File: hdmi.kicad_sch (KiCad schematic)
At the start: 11 parts, among them J2101 FPC0.5-SMT-20P, U2101 RCLAMP0524P, U2102 RCLAMP0524P, U2103 RCLAMP0524P, U3102 AP22653W6-7

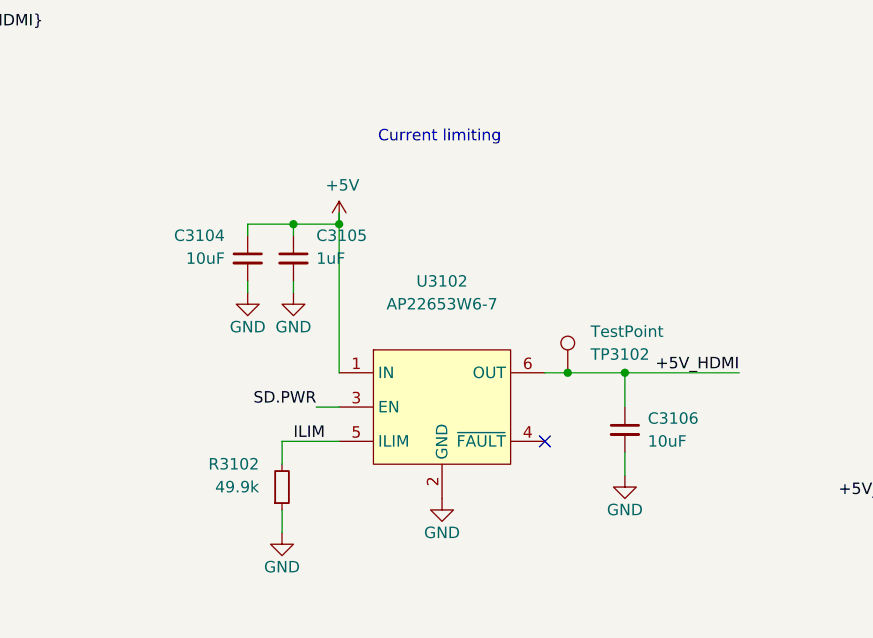
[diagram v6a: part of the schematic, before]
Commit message: Finish transitioning to RP2040
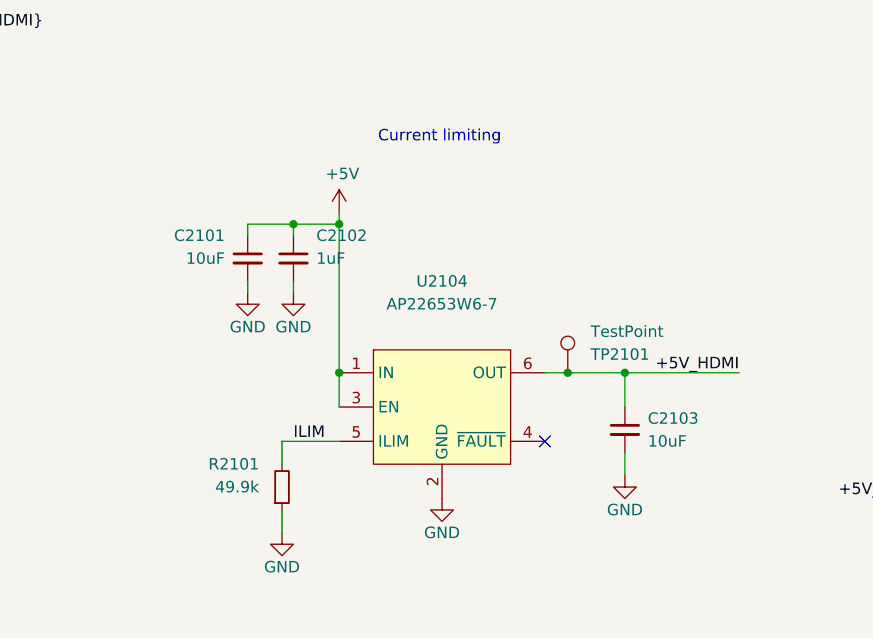
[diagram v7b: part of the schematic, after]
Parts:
- renumbered C3104 to C2101, C3105 to C2102, C3106 to C2103, R3102 to R2101, TP3102 to TP2101, U3102 to U2104
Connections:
- net SD.PWR is gone; now on net +5V: U2104.3 (EN)
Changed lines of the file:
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@@
 	)
 	(junction
+		(at 148.59 99.06)
+		(diameter 0)
+		(color 0 0 0 0)
+	)
+	(junction
 		(at 180.34 99.06)
 		(diameter 0.9144)
@@
 	(wire
 		(pts
-			(xy 146.05 102.87) (xy 148.59 102.87)
-		)
-		(stroke
-			(width 0)
-			(type default)
-		)
-	)
-	(wire
-		(pts
 			(xy 242.57 73.66) (xy 242.57 81.28)
 		)
@@
 	(wire
 		(pts
+			(xy 148.59 99.06) (xy 148.59 102.87)
+		)
+		(stroke
+			(width 0)
+			(type default)
+		)
+	)
+	(wire
+		(pts
 			(xy 213.36 113.03) (xy 217.17 113.03)
 		)
@@
 		)
 	)
-	(label "SD.PWR"
-		(at 146.05 102.87 180)
-		(effects
-			(font
-				(size 1.27 1.27)
-			)
-			(justify right bottom)
-		)
-	)
 	(label "HDMI.D0-"
 		(at 97.79 107.95 180)
@@
 		(dnp no)
 		(fields_autoplaced yes)
-		(property "Reference" "R3102"
+		(property "Reference" "R2101"
 			(at 139.7 109.2199 0)
 			(effects
@@
 			(project "HALPI2"
 				(path "/abc482bd-3f17-4d35-80db-1da3dcdb5c27/851e7ce4-d5b0-47f7-ace9-4a347f172348/49314faa-db35-4ef5-b0c8-5c327f44891d"
-					(reference "R3103")
+					(reference "R2201")
 					(unit 1)
 				)
 				(path "/abc482bd-3f17-4d35-80db-1da3dcdb5c27/851e7ce4-d5b0-47f7-ace9-4a347f172348/890900ed-b859-477a-afc8-e6aecd491b67"
-					(reference "R3102")
+					(reference "R2101")
 					(unit 1)
 				)
@@
 		(on_board yes)
 		(dnp no)
-		(property "Reference" "#PWR03110"
+		(property "Reference" "#PWR02105"
 			(at 142.24 123.19 0)
 			(effects
@@
 			(project "HALPI2"
 				(path "/abc482bd-3f17-4d35-80db-1da3dcdb5c27/851e7ce4-d5b0-47f7-ace9-4a347f172348/49314faa-db35-4ef5-b0c8-5c327f44891d"
-					(reference "#PWR03116")
+					(reference "#PWR02205")
 					(unit 1)
 				)
 				(path "/abc482bd-3f17-4d35-80db-1da3dcdb5c27/851e7ce4-d5b0-47f7-ace9-4a347f172348/890900ed-b859-477a-afc8-e6aecd491b67"
-					(reference "#PWR03110")
+					(reference "#PWR02105")
 					(unit 1)
 				)
@@
 		(on_board yes)
 		(dnp no)
-		(property "Reference" "#PWR02107"
+		(property "Reference" "#PWR02112"
 			(at 256.54 69.85 0)
 			(effects
@@
 			(project "HALPI2"
 				(path "/abc482bd-3f17-4d35-80db-1da3dcdb5c27/851e7ce4-d5b0-47f7-ace9-4a347f172348/49314faa-db35-4ef5-b0c8-5c327f44891d"
-					(reference "#PWR02207")
+					(reference "#PWR02212")
 					(unit 1)
 				)
 				(path "/abc482bd-3f17-4d35-80db-1da3dcdb5c27/851e7ce4-d5b0-47f7-ace9-4a347f172348/890900ed-b859-477a-afc8-e6aecd491b67"
-					(reference "#PWR02107")
+					(reference "#PWR02112")
 					(unit 1)
 				)
@@
 		(on_board yes)
 		(dnp no)
-		(property "Reference" "#PWR02106"
+		(property "Reference" "#PWR02111"
 			(at 242.57 133.35 0)
 			(effects
@@
 			(project "HALPI2"
 				(path "/abc482bd-3f17-4d35-80db-1da3dcdb5c27/851e7ce4-d5b0-47f7-ace9-4a347f172348/49314faa-db35-4ef5-b0c8-5c327f44891d"
-					(reference "#PWR02206")
+					(reference "#PWR02211")
 					(unit 1)
 				)
 				(path "/abc482bd-3f17-4d35-80db-1da3dcdb5c27/851e7ce4-d5b0-47f7-ace9-4a347f172348/890900ed-b859-477a-afc8-e6aecd491b67"
-					(reference "#PWR02106")
+					(reference "#PWR02111")
 					(unit 1)
 				)
@@
 		(dnp no)
 		(fields_autoplaced yes)
-		(property "Reference" "U3102"
+		(property "Reference" "U2104"
 			(at 160.02 88.9 0)
 			(effects
@@
 			(project "HALPI2"
 				(path "/abc482bd-3f17-4d35-80db-1da3dcdb5c27/851e7ce4-d5b0-47f7-ace9-4a347f172348/49314faa-db35-4ef5-b0c8-5c327f44891d"
-					(reference "U3103")
+					(reference "U2204")
 					(unit 1)
 				)
 				(path "/abc482bd-3f17-4d35-80db-1da3dcdb5c27/851e7ce4-d5b0-47f7-ace9-4a347f172348/890900ed-b859-477a-afc8-e6aecd491b67"
-					(reference "U3102")
+					(reference "U2104")
 					(unit 1)
 				)
@@
 		(on_board yes)
 		(dnp no)
-		(property "Reference" "TP3102"
+		(property "Reference" "TP2101"
 			(at 176.53 97.0281 0)
 			(effects
@@
 			(project "HALPI2"
 				(path "/abc482bd-3f17-4d35-80db-1da3dcdb5c27/851e7ce4-d5b0-47f7-ace9-4a347f172348/49314faa-db35-4ef5-b0c8-5c327f44891d"
-					(reference "TP3103")
+					(reference "TP2201")
 					(unit 1)
 				)
 				(path "/abc482bd-3f17-4d35-80db-1da3dcdb5c27/851e7ce4-d5b0-47f7-ace9-4a347f172348/890900ed-b859-477a-afc8-e6aecd491b67"
-					(reference "TP3102")
+					(reference "TP2101")
 					(unit 1)
 				)
@@
 		(on_board yes)
 		(dnp no)
-		(property "Reference" "C3106"
+		(property "Reference" "C2103"
 			(at 182.88 104.14 0)
 			(effects
@@
 			(project "HALPI2"
 				(path "/abc482bd-3f17-4d35-80db-1da3dcdb5c27/851e7ce4-d5b0-47f7-ace9-4a347f172348/49314faa-db35-4ef5-b0c8-5c327f44891d"
-					(reference "C3109")
+					(reference "C2203")
 					(unit 1)
 				)
 				(path "/abc482bd-3f17-4d35-80db-1da3dcdb5c27/851e7ce4-d5b0-47f7-ace9-4a347f172348/890900ed-b859-477a-afc8-e6aecd491b67"
-					(reference "C3106")
+					(reference "C2103")
 					(unit 1)
 				)
@@
 		(on_board yes)
 		(dnp no)
-		(property "Reference" "#PWR02105"
+		(property "Reference" "#PWR02110"
 			(at 217.17 133.35 0)
 			(effects
@@
 			(project "HALPI2"
 				(path "/abc482bd-3f17-4d35-80db-1da3dcdb5c27/851e7ce4-d5b0-47f7-ace9-4a347f172348/49314faa-db35-4ef5-b0c8-5c327f44891d"
-					(reference "#PWR02205")
+					(reference "#PWR02210")
 					(unit 1)
 				)
 				(path "/abc482bd-3f17-4d35-80db-1da3dcdb5c27/851e7ce4-d5b0-47f7-ace9-4a347f172348/890900ed-b859-477a-afc8-e6aecd491b67"
-					(reference "#PWR02105")
+					(reference "#PWR02110")
 					(unit 1)
 				)
@@
 		(dnp no)
 		(fields_autoplaced yes)
-		(property "Reference" "C3105"
+		(property "Reference" "C2102"
 			(at 146.05 83.8262 0)
 			(effects
@@
 			(project "HALPI2"
 				(path "/abc482bd-3f17-4d35-80db-1da3dcdb5c27/851e7ce4-d5b0-47f7-ace9-4a347f172348/49314faa-db35-4ef5-b0c8-5c327f44891d"
-					(reference "C3108")
+					(reference "C2202")
 					(unit 1)
 				)
 				(path "/abc482bd-3f17-4d35-80db-1da3dcdb5c27/851e7ce4-d5b0-47f7-ace9-4a347f172348/890900ed-b859-477a-afc8-e6aecd491b67"
-					(reference "C3105")
+					(reference "C2102")
 					(unit 1)
 				)
@@
 		(on_board yes)
 		(dnp no)
-		(property "Reference" "#PWR03114"
+		(property "Reference" "#PWR02109"
 			(at 180.34 116.84 0)
 			(effects
@@
 			(project "HALPI2"
 				(path "/abc482bd-3f17-4d35-80db-1da3dcdb5c27/851e7ce4-d5b0-47f7-ace9-4a347f172348/49314faa-db35-4ef5-b0c8-5c327f44891d"
-					(reference "#PWR03120")
+					(reference "#PWR02209")
 					(unit 1)
 				)
 				(path "/abc482bd-3f17-4d35-80db-1da3dcdb5c27/851e7ce4-d5b0-47f7-ace9-4a347f172348/890900ed-b859-477a-afc8-e6aecd491b67"
-					(reference "#PWR03114")
+					(reference "#PWR02109")
 					(unit 1)
 				)
@@
 		(on_board yes)
 		(dnp no)
-		(property "Reference" "#PWR03113"
+		(property "Reference" "#PWR02108"
 			(at 160.02 119.38 0)
 			(effects
@@
 			(project "HALPI2"
 				(path "/abc482bd-3f17-4d35-80db-1da3dcdb5c27/851e7ce4-d5b0-47f7-ace9-4a347f172348/49314faa-db35-4ef5-b0c8-5c327f44891d"
-					(reference "#PWR03119")
+					(reference "#PWR02208")
 					(unit 1)
 				)
 				(path "/abc482bd-3f17-4d35-80db-1da3dcdb5c27/851e7ce4-d5b0-47f7-ace9-4a347f172348/890900ed-b859-477a-afc8-e6aecd491b67"
-					(reference "#PWR03113")
+					(reference "#PWR02108")
 					(unit 1)
 				)
@@
 		(on_board yes)
 		(dnp no)
-		(property "Reference" "C3104"
+		(property "Reference" "C2101"
 			(at 135.89 83.8262 0)
 			(effects
@@
 			(project "HALPI2"
 				(path "/abc482bd-3f17-4d35-80db-1da3dcdb5c27/851e7ce4-d5b0-47f7-ace9-4a347f172348/49314faa-db35-4ef5-b0c8-5c327f44891d"
-					(reference "C3107")
+					(reference "C2201")
 					(unit 1)
 				)
 				(path "/abc482bd-3f17-4d35-80db-1da3dcdb5c27/851e7ce4-d5b0-47f7-ace9-4a347f172348/890900ed-b859-477a-afc8-e6aecd491b67"
-					(reference "C3104")
+					(reference "C2101")
 					(unit 1)
 				)
@@
 	(symbol
 		(lib_id "power:+5V")
-		(at 148.59 82.55 0)
+		(at 148.59 81.28 0)
 		(unit 1)
 		(exclude_from_sim no)
@@
 		(on_board yes)
 		(dnp no)
-		(property "Reference" "#PWR02108"
-			(at 148.59 86.36 0)
+		(property "Reference" "#PWR02107"
+			(at 148.59 85.09 0)
 			(effects
 				(font
@@
 		)
 		(property "Value" "+5V"
-			(at 148.9583 78.2256 0)
+			(at 148.9583 76.9556 0)
 			(effects
 				(font
@@
 		)
 		(property "Footprint" ""
-			(at 148.59 82.55 0)
+			(at 148.59 81.28 0)
 			(effects
 				(font
@@
 		)
 		(property "Datasheet" ""
-			(at 148.59 82.55 0)
+			(at 148.59 81.28 0)
 			(effects
 				(font
@@
 		)
 		(property "Description" "Power symbol creates a global label with name \"+5V\""
-			(at 148.59 82.55 0)
+			(at 148.59 81.28 0)
 			(effects
 				(font
@@
 			(project "HALPI2"
 				(path "/abc482bd-3f17-4d35-80db-1da3dcdb5c27/851e7ce4-d5b0-47f7-ace9-4a347f172348/49314faa-db35-4ef5-b0c8-5c327f44891d"
-					(reference "#PWR02109")
+					(reference "#PWR02207")
 					(unit 1)
 				)
 				(path "/abc482bd-3f17-4d35-80db-1da3dcdb5c27/851e7ce4-d5b0-47f7-ace9-4a347f172348/890900ed-b859-477a-afc8-e6aecd491b67"
-					(reference "#PWR02108")
+					(reference "#PWR02107")
 					(unit 1)
 				)
@@
 		(on_board yes)
 		(dnp no)
-		(property "Reference" "#PWR03109"
+		(property "Reference" "#PWR02104"
 			(at 138.43 96.52 0)
 			(effects
@@
 			(project "HALPI2"
 				(path "/abc482bd-3f17-4d35-80db-1da3dcdb5c27/851e7ce4-d5b0-47f7-ace9-4a347f172348/49314faa-db35-4ef5-b0c8-5c327f44891d"
-					(reference "#PWR03115")
+					(reference "#PWR02204")
 					(unit 1)
 				)
 				(path "/abc482bd-3f17-4d35-80db-1da3dcdb5c27/851e7ce4-d5b0-47f7-ace9-4a347f172348/890900ed-b859-477a-afc8-e6aecd491b67"
-					(reference "#PWR03109")
+					(reference "#PWR02104")
 					(unit 1)
 				)
@@
 		(on_board yes)
 		(dnp no)
-		(property "Reference" "#PWR03111"
+		(property "Reference" "#PWR02106"
 			(at 143.51 96.52 0)
 			(effects
@@
 			(project "HALPI2"
 				(path "/abc482bd-3f17-4d35-80db-1da3dcdb5c27/851e7ce4-d5b0-47f7-ace9-4a347f172348/49314faa-db35-4ef5-b0c8-5c327f44891d"
-					(reference "#PWR03117")
+					(reference "#PWR02206")
 					(unit 1)
 				)
 				(path "/abc482bd-3f17-4d35-80db-1da3dcdb5c27/851e7ce4-d5b0-47f7-ace9-4a347f172348/890900ed-b859-477a-afc8-e6aecd491b67"
-					(reference "#PWR03111")
+					(reference "#PWR02106")
 					(unit 1)
 				)

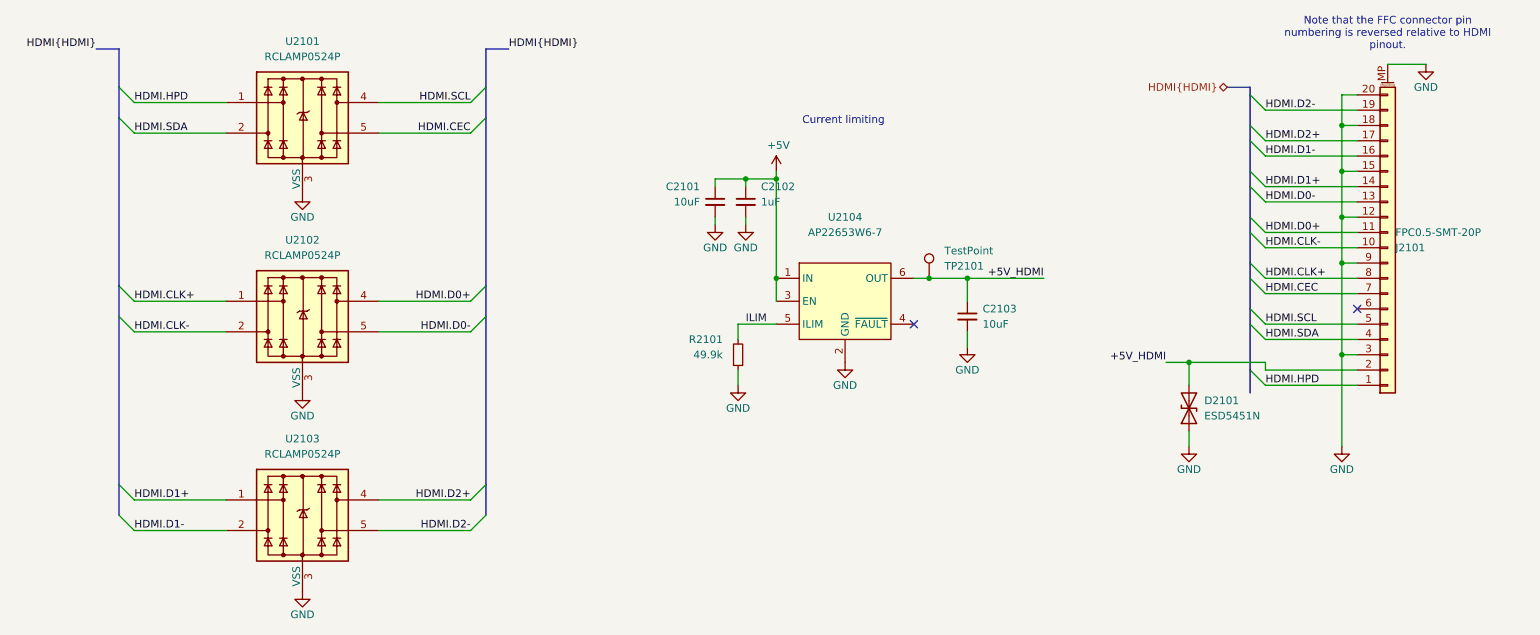
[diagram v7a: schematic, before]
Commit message: Apply part PCBA position corrections
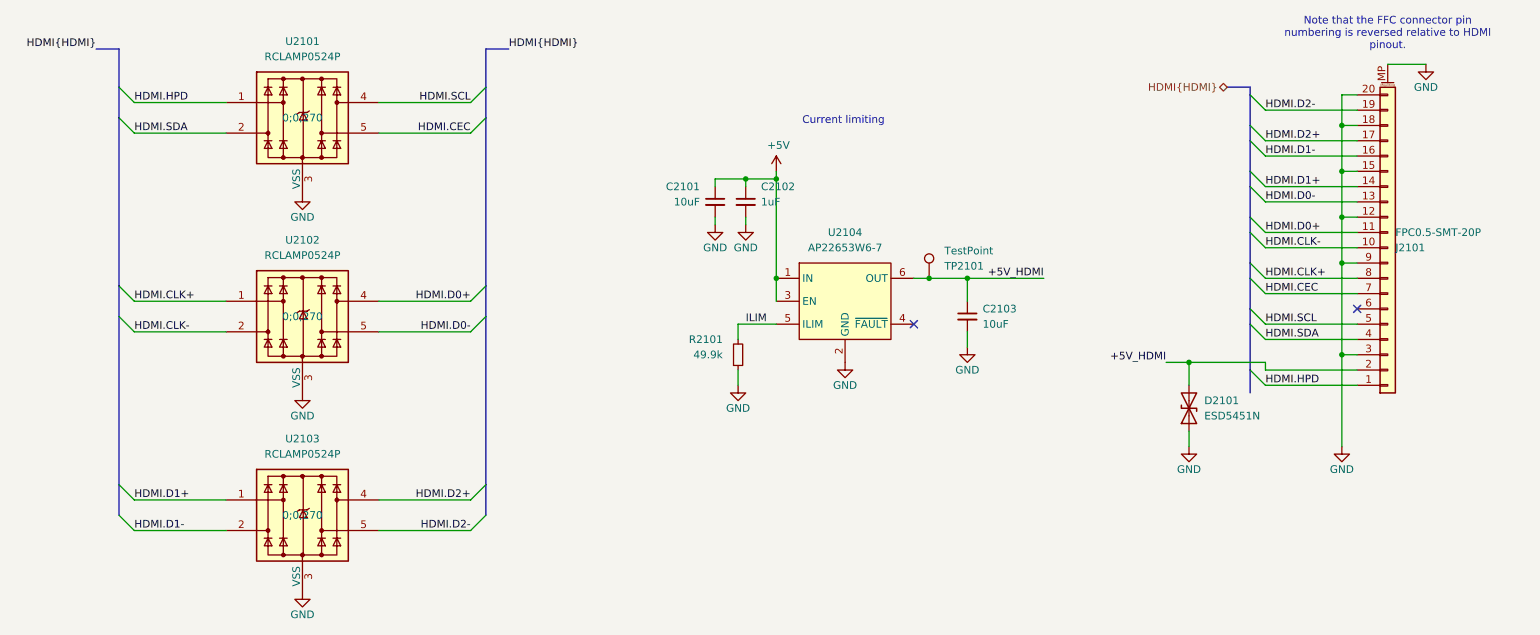
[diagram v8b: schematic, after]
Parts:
- U2101, U2102, U2103: JLCPCB_CORRECTION (none) -> 0;0;270
- U2104: JLCPCB_CORRECTION (none) -> 0;0;180
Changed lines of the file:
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@@
+			)
+		)
+		(property "JLCPCB_CORRECTION" "0;0;270"
+			(at 69.85 105.41 0)
+			(effects
+				(font
+					(size 1.27 1.27)
+				)
 			)
 		)
@@
 		(fields_autoplaced yes)
 		(property "Reference" "U2104"
-			(at 160.02 88.9 0)
+			(at 160.02 91.44 0)
 			(effects
 				(font
@@
 		)
 		(property "Value" "AP22653W6-7"
-			(at 160.02 91.44 0)
+			(at 160.02 93.98 0)
 			(effects
 				(font
@@
 					(size 1.27 1.27)
 				)
+			)
+		)
+		(property "JLCPCB_CORRECTION" "0;0;180"
+			(at 160.02 102.87 0)
+			(effects
+				(font
+					(size 1.27 1.27)
+				)
+				(hide yes)
 			)
 		)
@@
 			)
 		)
+		(property "JLCPCB_CORRECTION" "0;0;270"
+			(at 69.85 72.39 0)
+			(effects
+				(font
+					(size 1.27 1.27)
+				)
+			)
+		)
 		(pin "1"
 		)
@@
 			(at 69.85 138.43 0)
 			(effects
+				(font
+					(size 1.27 1.27)
+				)
+			)
+		)
+		(property "JLCPCB_CORRECTION" "0;0;270"
+			(at 69.85 138.43 0)
+			(effects
